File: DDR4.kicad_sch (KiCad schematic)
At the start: 39 parts, among them U14 2199155-1

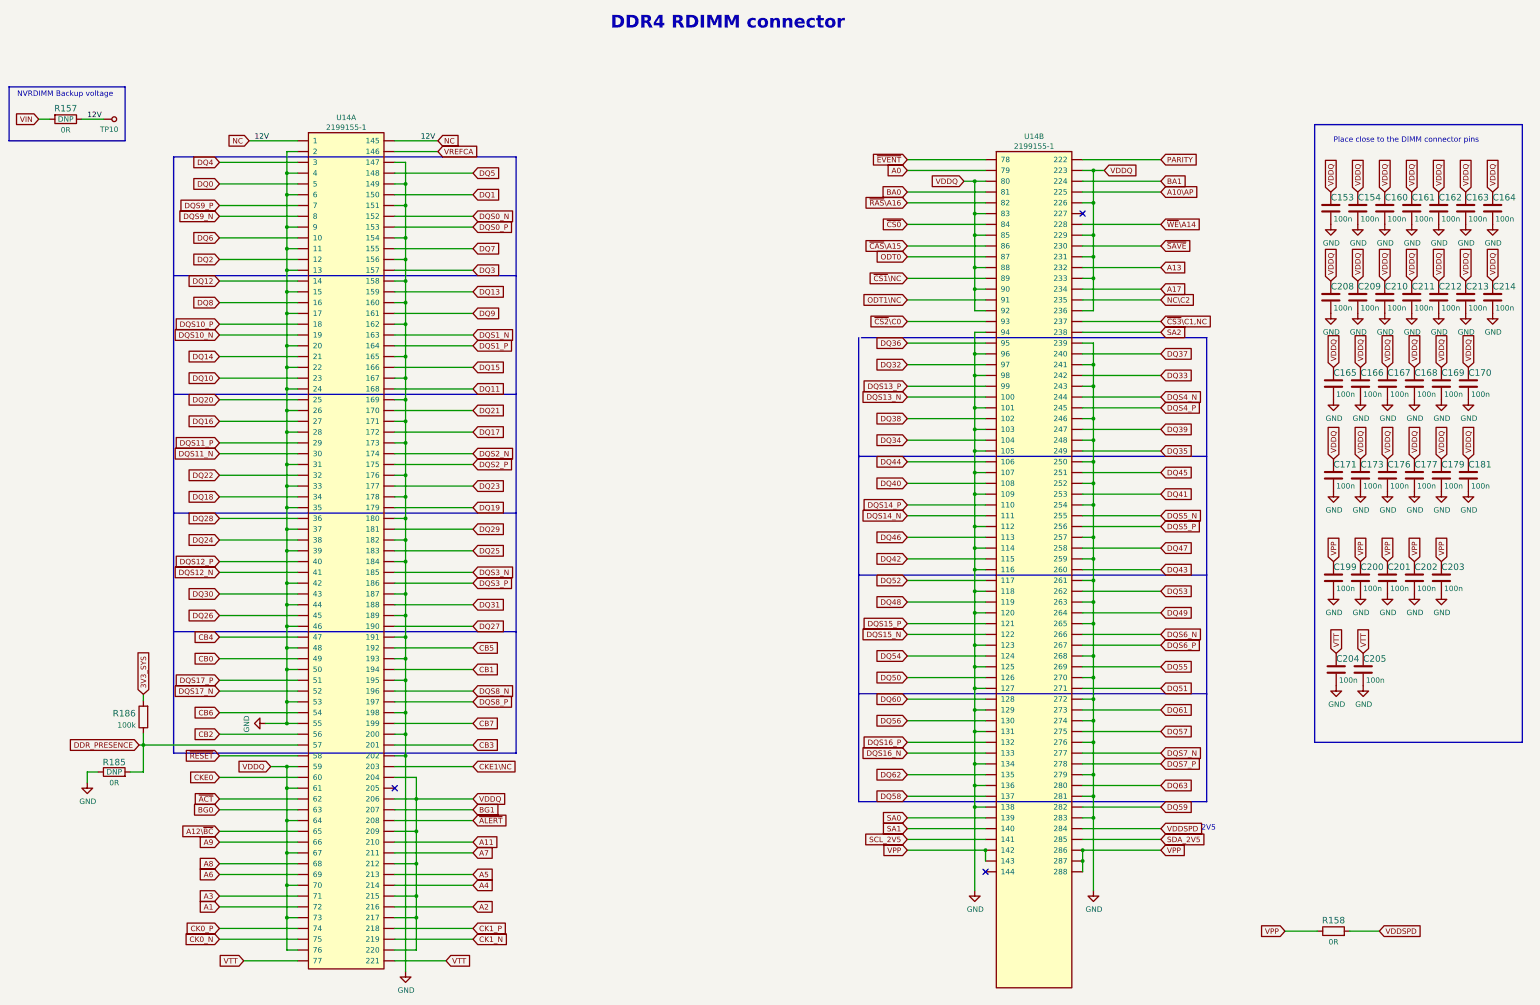
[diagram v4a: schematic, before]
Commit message: Implement all review fixes, route control signals from FMC to FPGA
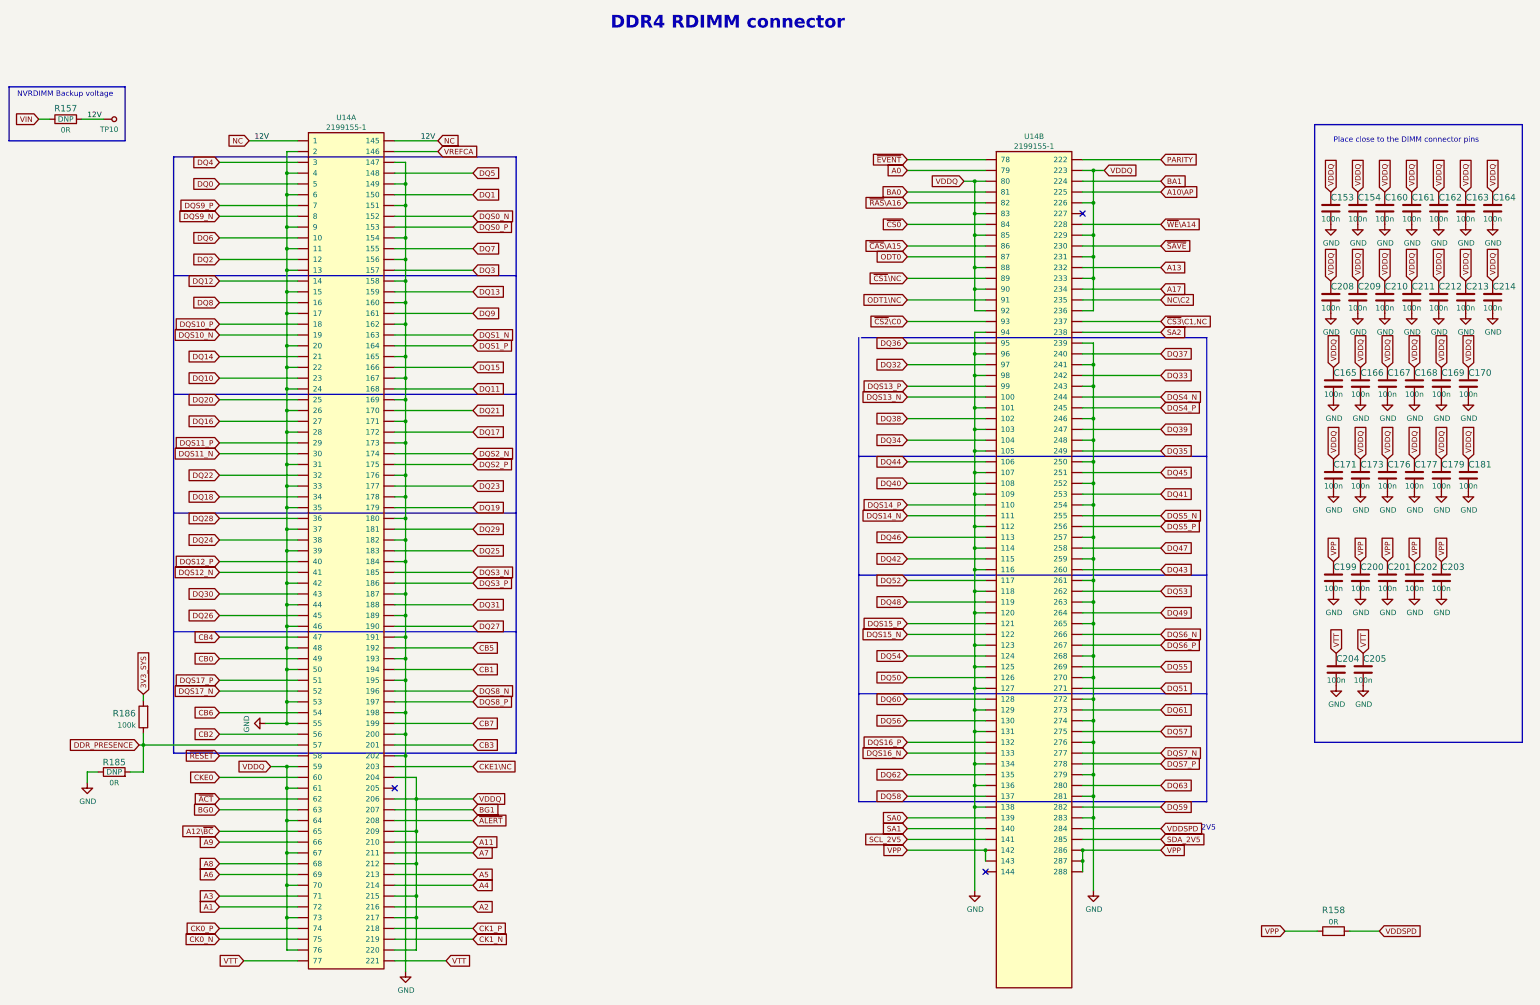
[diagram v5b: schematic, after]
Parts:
- removed R157, R158: R_0R_0603, data-center-dram-tester-footprints:0603-res, symbol data-center-dram-tester:R_0R_0603
- added R157, R158: R_0R_0402, antmicro-footprints:0402-res, symbol antmicroResistors0402:R_0R_0402
- C153, C154, C160, C161, C162, C163, C164, C165, C166, C167, C168, C169, C170, C171, C173, C176, C177, C179, C181, C199, C200, C201, C202, C203, C204, C205, C208, C209, C210, C211, C212, C213, C214: value C_100n_0402_6V3 -> C_100n_0402; footprint data-center-dram-tester-footprints:0402-cap -> antmicro-footprints:0402-cap; symbol data-center-dram-tester:C_100n_0402_6V3 -> antmicroCapacitors0402:C_100n_0402; MPN 0402X104K6R3CT -> GRM155R61H104KE14D; Manufacturer Walsin -> Murata
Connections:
- net NC: now also R157.2
- net VDDSPD: now also R158.2
- net VIN: now also R157.1
- net VPP: now also R158.1
